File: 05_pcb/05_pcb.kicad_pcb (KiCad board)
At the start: 2 copper layers, 24 parts, among them J1 MPU6050, J2 USB_C_Receptacle_USB2.0_16P, SW1 SW_Nidec_CAS-120A1, U1 ATmega328P-A, U2 W25Q128JVS, U3 CH340C, U4 MCP73831-2-OT, U5 MCP1700x-330xxTT

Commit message: PCB complete
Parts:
- moved BT1 106.5 mm to (155.2, 93.4)
- moved C2 106.3 mm to (135.3, 117.9)
- moved U5 106.0 mm to (130.5, 118.2)
- moved C1 104.8 mm to (147.0, 92.8)
- moved C4 104.8 mm to (134.6, 97.3)
- moved C6 104.8 mm to (133.3, 78.2)
- moved J1 104.8 mm to (129.2, 78.2)
- moved R1 104.8 mm to (133.0, 113.1)
- moved R3 104.8 mm to (136.5, 107.4)
- moved R4 104.8 mm to (152.4, 103.0)
- moved R5 104.8 mm to (136.5, 82.7)
- moved R6 104.8 mm to (138.9, 77.6)
- moved R7 104.8 mm to (152.4, 97.9)
- moved SW1 104.8 mm to (156.4, 117.1)
- moved U1 104.8 mm to (146.5, 82.0)
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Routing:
- net Vcc: track 37.0 -> 101.1 mm, vias 0 -> 4
- net CS: track 0.00 -> 37.0 mm, vias 0 -> 2
- net CLK: track 0.00 -> 36.4 mm, vias 0 -> 2
- net MOSI: track 0.00 -> 35.8 mm, vias 0 -> 2
- net RST: track 0.00 -> 34.1 mm, vias 0 -> 4
- net MISO: track 0.00 -> 32.8 mm, vias 0 -> 2
- net INT: track 0.00 -> 27.5 mm, vias 0 -> 2
- net SDA: track 0.00 -> 26.3 mm, vias 0 -> 2
- net Net-(SW1-A): track 0.00 -> 26.3 mm
- net SCL: track 0.00 -> 24.5 mm, vias 0 -> 2
- net Net-(J2-CC1): track 0.00 -> 20.2 mm, vias 0 -> 2
- net D-: track 0.00 -> 20.2 mm, vias 0 -> 3
- net Vbus: track 37.6 -> 57.3 mm
- net Net-(U3-RXD): track 0.00 -> 19.7 mm, vias 0 -> 2
- net D+: track 0.00 -> 14.2 mm, vias 0 -> 2
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- added copper zone on B.Cu, net GND
- added copper zone on F.Cu, net GND
- added copper zone on F.Cu, net Vbus
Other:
- board outline added: 32.6 x 46 mm
- board text added: "IMU_TF_v1"

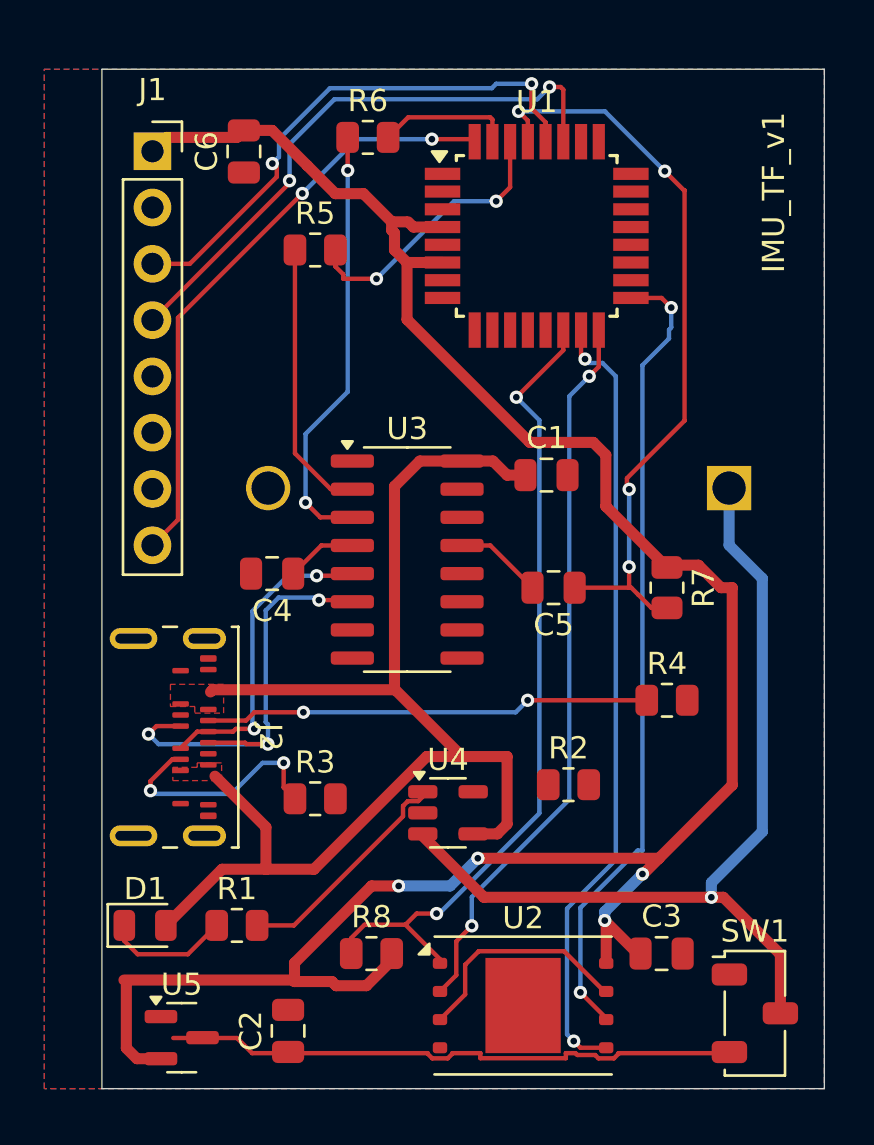
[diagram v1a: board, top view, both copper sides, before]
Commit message: New switch footprint and USBC connector
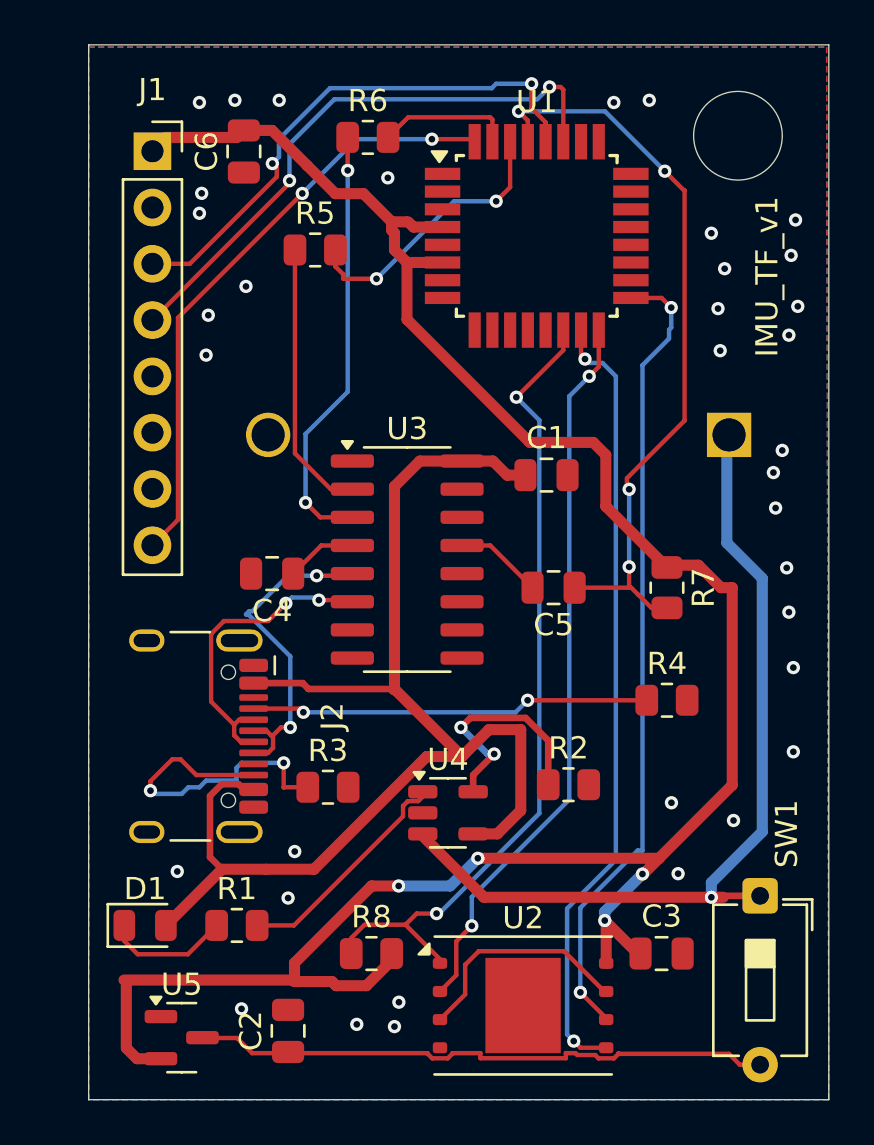
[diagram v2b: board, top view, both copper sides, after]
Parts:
- J2: footprint Connector_USB:USB_C_Receptacle_Amphenol_124019772112A -> Connector_USB:USB_C_Receptacle_HCTL_HC-TYPE-C-16P-01A
- SW1: value SW_Nidec_CAS-120A1 -> SW_DPST_x2; footprint Button_Switch_SMD:Nidec_Copal_CAS-120A -> Button_Switch_THT:SW_DIP_SPSTx01_Slide_6.7x4.1mm_W7.62mm_P2.54mm_LowProfile
- moved SW1 5.31 mm to (156.6, 111.8), turned to -90 degrees
- moved BT1 2.40 mm to (155.2, 91.0)
- moved J2 1.50 mm to (130.0, 104.6)
- moved R3 0.78 mm to (137.1, 106.9)
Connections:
- C2 pad 1: Net-(SW1-A) -> Net-(SW1A-B)
- SW1 pad 1: unconnected-(SW1-C-Pad1) -> Vbat
- SW1 pad 2: Vbat -> Net-(SW1A-B)
- U5 pad 3: Net-(SW1-A) -> Net-(SW1A-B)
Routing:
- net Net-(SW1A-B): track 0.00 -> 26.5 mm
- net Net-(SW1-A): track 26.3 -> 0.00 mm
- net Net-(U4-PROG): track 0.00 -> 10.6 mm, vias 0 -> 2
- net D-: track 20.2 -> 14.1 mm, vias 3 -> 2
- net Net-(J2-CC2): track 10.7 -> 15.0 mm
- net Net-(J2-CC1): track 20.2 -> 18.1 mm
- net Vbat: track 41.0 -> 39.5 mm
- net Vbus: track 57.3 -> 58.8 mm
- net D+: track 14.2 -> 15.0 mm
- net GND: vias 0 -> 36
- removed copper zone on F.Cu, net Vbus
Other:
- board size 32.6 x 46 mm -> 33.4 x 47.6 mm
